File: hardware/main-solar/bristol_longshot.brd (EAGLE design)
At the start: 14 x 64 mm, 84 parts, among them U1 SAM_D20E, U10 SPV1040, U11 LT4054ES5-4.2, U12 TPS62243, U13 TPS62243, U14 TPS3808, U15 74LVC1G04GW, U2 SI4060, U3 UBLOX_MAX, U4 SST25WF040BT-40I/NP, U5 TG-5006CJ, U6 TG-5006CJ, U7 TPS3123, U8 SN74LVC1G32DCKR, U9 SE880, Y1 ABS05

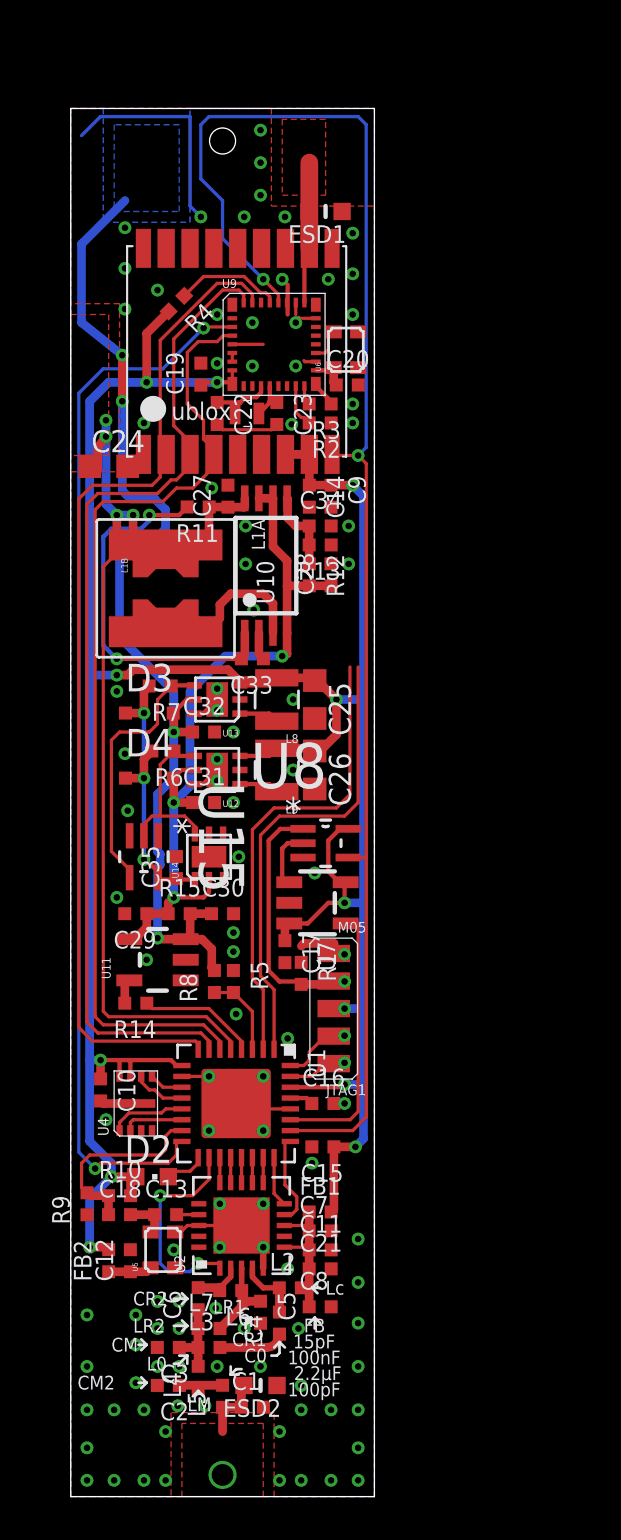
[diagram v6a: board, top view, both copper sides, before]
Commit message: Updated main tracker solar design to use a LTC3105 energy harvester for solar and a 3V primary lithium for backup. Work in Progress
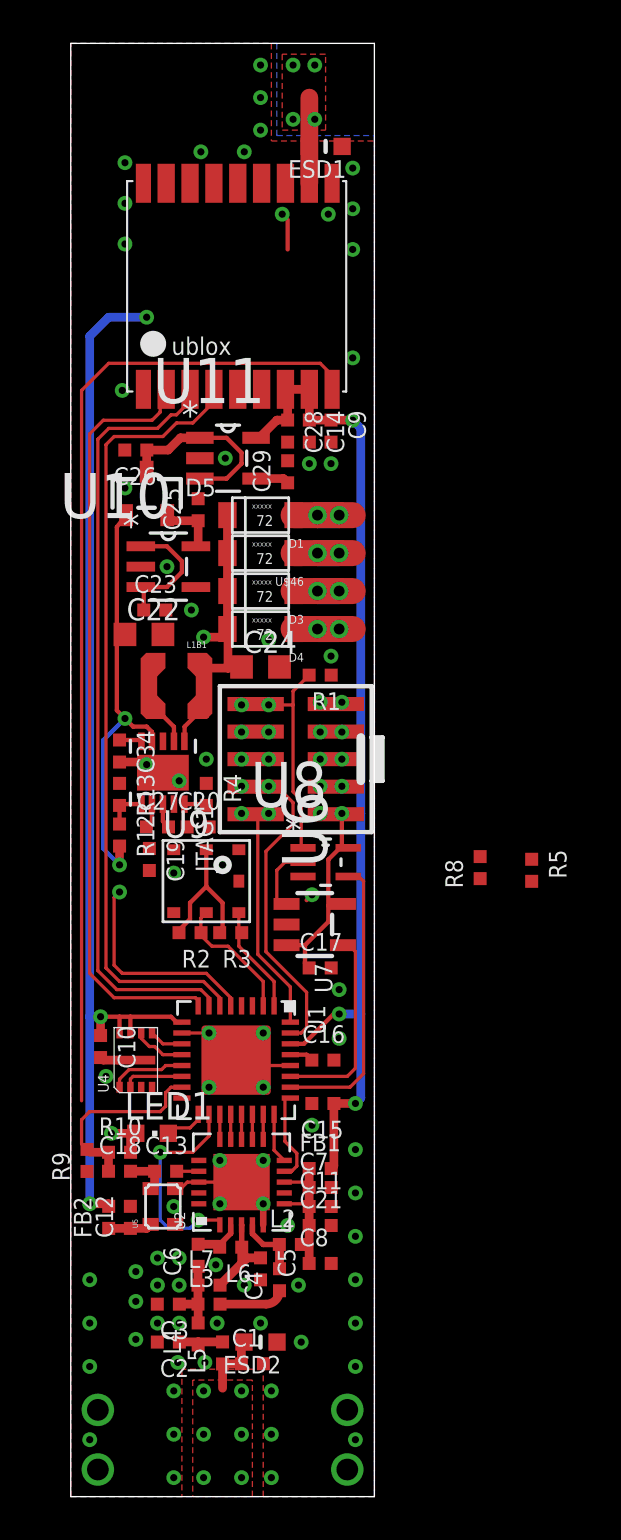
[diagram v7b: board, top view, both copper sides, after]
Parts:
- removed C30, C31, C32: 4.7µF, microbuilder_v3:_0402
- removed C33, C35: 1nF, microbuilder_v3:_0402
- removed D2: GREEN, led:CHIPLED_0603
- removed L1A: XAL6060, XAL6060:XAL60
- removed L1B: 10uH LPS3015, PecanFemto4:LPS3015
- removed L8, L9: 2.2µH, SparkFun:1007
- removed R11: 1kΩ, microbuilder_v3:_0402
- removed R14: 2.2kΩ, microbuilder_v3:_0402
- removed R15: 0Ω/DNP, microbuilder_v3:_0402
- removed R6, R7: 10kΩ, microbuilder_v3:_0402
- removed U12, U13: TPS62243, TPS62243:S-PWSON-N6
- removed U14: TPS3808, TPS3808:S-PWSON-N6
- removed U15: 74LVC1G04GW, 74LVC1G04GW_inverter:SOT65P210X110-5N
- removed Y1: ABS05, fbri:ABS05
- added D1, U$46: RB161M, RB161M:RB161M
- added D5: (no value), microbuilder_v3:SOT23-R
- added L1B1: 10uH LPS3015, PecanFemto4:LPS3015
- added LED1: GREEN, led:CHIPLED_0603
- C20: value 100nF -> 4.7µF
- C22: value 18pF -> 10µF; device microbuilder_v3:_0402 -> resistor:C0603K
- C23: value 18pF -> 1µF
- C25, C26: value 10µF -> 1µF; device resistor:C0603K -> microbuilder_v3:_0402
- C28: value 4.7µF -> 1µF
- C29: value 4.7µF -> 100nF
- C34: value 1nF -> 1µF
- D3, D4: value BAT760 -> RB161M; device BAT760:SOD323 -> RB161M:RB161M
- JTAG1: value M05 -> (none); device fbri:M05_SIDE -> microbuilder_v3:2X05_1.27MM_SMT
- R4: value 10kΩ -> 75kΩ
- U10: value SPV1040 -> LD6836TD/23P; device spv1040:TSSOP8 -> LD6836TD_23:SOT95P275X110-5N
- U11: value LT4054ES5-4.2 -> TPS73118DBVT; device XYKlib:SOT23-5 -> TPS73118DVBT:SOT95P280X145-5N
- U6: value TG-5006CJ -> LTC3105EDDPBF; device fbri:TC-5006CJ -> ltc3105:DFN300X300X80-11N
- U9: value SE880 -> BMP180; device fbri:SE880 -> SparkFun-Sensors:BMP180
- moved U9 24.9 mm to (6.25, 28.4)
- moved R3 24.7 mm to (7.38, 26.0)
- moved R2 24.3 mm to (5.50, 26.0)
- moved U11 23.4 mm to (7.25, 47.9), turned to 0 degrees
- moved R4 22.7 mm to (6.25, 32.4), turned to 270 degrees
- moved C19 22.5 mm to (3.62, 29.4), turned to 270 degrees
- moved C29 21.5 mm to (10.0, 47.2), turned to 90 degrees
- moved C20 21.5 mm to (5.88, 30.9)
- moved U6 21.2 mm to (4.25, 33.4)
- moved C26 16.9 mm to (3.00, 48.2), turned to 180 degrees
- moved C27 15.6 mm to (4.00, 30.9), turned to 0 degrees
- moved R12 14.9 mm to (2.25, 30.5)
- moved R13 14.8 mm to (2.25, 32.4), turned to 270 degrees
- moved R5 14.7 mm to (21.2, 28.9)
- moved C34 13.9 mm to (2.25, 34.4), turned to 270 degrees
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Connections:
- removed net BATTERY_BUCK_SW: L8.1, U13.1
- removed net BATTERY_EN: R7.1, U13.4, U15.4
- removed net CHG_STATUS: U11.1
- removed net CT: U14.3
- removed net LED2: D2.C, U1.17
- removed net LX1: L1A.P$2, L1B.2_1, L1B.2_2, L1B.2_3, L1B.2_4, L1B.2_5, L1B.2_6, L1B.2_7, L1B.2_8, L1B.2_9, U10.3
- removed net MPP-SET: C33.2, R11.2, U10.1
- removed net MPPT-VOUT-TANK: C28.1, C29.1, C31.1, D4.A, R12.2, R15.1, U10.4, U10.6, U10.7, U11.4, U12.5, U14.2
- removed net N$3: R3.2, U9.$17
- removed net N$5: R2.2, U9.$16
- removed net PROG: R14.2, U11.5
- removed net RTC_XI: C22.1, U9.$12, Y1.1
- removed net RTC_XO: C23.1, U9.$13, Y1.2
- removed net SE_MODE_PULL: R4.1, U9.$31
- removed net SE_ON_OFF: U1.16, U9.$3
- removed net SE_TCXO_CLK: U6.3, U9.$21
- removed net SE_VCO_TCXO: C20.1, U6.4, U9.$19
- removed net SE_VREG: U9.$6, U9.$7
- removed net SPV_VCTRL1: C34.1, R12.1, R13.2, U10.5
- removed net SUPERVISOR_VCC: C35.1, D3.C, D4.C, R6.2, R7.2, U14.1, U15.5
- removed net TANK_BUCK_SW: L9.1, U12.1
- removed net TANK_EN: R6.1, U12.4, U14.6, U15.2
- removed net VSOLAR: C24.1, C27.1, L1A.P$1, L1B.1_1, L1B.1_2, L1B.1_3, L1B.1_4, L1B.1_5, L1B.1_6, L1B.1_7, L1B.1_8, L1B.1_9, R11.1, U1.5, U10.8
- new net BATTERY_LDO_OUT: C25.1, D5.2, U10.5
- new net BATTERY_P: C23.1, U10.1, U10.3
- new net GPS_!RESET: U1.16, U3.9_V_RESET
- new net LED1: LED1.C, U1.17
- new net MPPT_AUX: C34.1, U6.10
- new net MPPT_FB: R12.1, R13.2, U6.1
- new net MPPT_LDO: C27.1, U6.2
- new net MPPT_SET: R4.2, U6.5
- new net MPPT_SW: L1B1.2_1, L1B1.2_2, L1B1.2_3, L1B1.2_4, L1B1.2_5, L1B1.2_6, L1B1.2_7, L1B1.2_8, L1B1.2_9, U6.7
- new net NR: C29.1, U11.4
- new net PANEL_1: D1.ANODE
- new net PANEL_2: U$46.ANODE
- new net PANEL_3: D3.ANODE
- new net PANEL_4: D4.ANODE
- new net SCHOTTY_COMB_OUT: C26.1, D5.3, U11.1, U11.3
- new net SOLAR: C24.1, D1.CATHODE, D3.CATHODE, D4.CATHODE, L1B1.1_1, L1B1.1_2, L1B1.1_3, L1B1.1_4, L1B1.1_5, L1B1.1_6, L1B1.1_7, L1B1.1_8, L1B1.1_9, U$46.CATHODE, U1.5, U6.6
- new net SOLAR_MPPT_OUT: C22.1, D5.1, R12.2, U6.9
- net !RESET: no longer U3.9_V_RESET, U9.$30
- net 1.8V: now also C20.1, C28.1, JTAG1.1, LED1.A, R2.2, R3.2, U11.5, U9.2, U9.3; no longer C25.1, C26.1, D2.A, JTAG1.$3, L8.2, L9.2, R4.2, U12.3, U13.3, U9.$8, U9.$9
- net BATTERY: no longer C30.1, C32.1, D3.A, R15.2, U11.3, U13.5
- net CHG_CONTROL: no longer R14.1
- net EXT!RESET: now also JTAG1.10; no longer JTAG1.$2
- net GIMO: no longer U9.$34
- net GND: now also JTAG1.3, JTAG1.5, R4.1, U6.11, U6.3, U9.7; no longer C30.2, C31.2, C32.2, C33.1, C35.2, JTAG1.$1, R2.1, R3.1, U12.2, U12.6, U12.PAD, U13.2, U13.6, U13.PAD, U14.5, U14.PAD, U15.3, U6.2, U9.$1, U9.$18, U9.$20, U9.$23, U9.$24, U9.$25, U9.$26, U9.$28, U9.$29, U9.$5
- net GOMI: no longer U9.$33
- net GPS_ANT: no longer U9.$27
- net SCL: now also R2.1, U9.5
- net SDA: now also R3.1, U9.6
- net SWDCLK: now also JTAG1.4; no longer JTAG1.$5
- net SWDIO: now also JTAG1.2; no longer JTAG1.$4
- net TIMEPULSE: no longer U9.$4
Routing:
- net !RESET: track 69.5 -> 13.3 mm, vias 2 -> 0
- net VSOLAR: track 53.3 -> 0.00 mm, vias 4 -> 0
- net BATTERY: track 49.3 -> 0.00 mm, vias 4 -> 0
- net SE_ON_OFF: track 49.3 -> 0.00 mm, vias 2 -> 0
- net GPS_!RESET: track 0.00 -> 45.7 mm
- net MPPT-VOUT-TANK: track 34.0 -> 0.00 mm, vias 3 -> 0
- net SOLAR: track 0.00 -> 26.7 mm, vias 0 -> 2
- net GND: track 39.6 -> 18.2 mm, vias 105 -> 85
- net SOLAR_MPPT_OUT: track 0.00 -> 20.3 mm, vias 0 -> 2
- net MPP-SET: track 17.5 -> 0.00 mm, vias 2 -> 0
- net 1.8V: track 137.5 -> 120.7 mm, vias 12 -> 9
- net SDA: track 21.5 -> 5.22 mm
- net SCL: track 21.4 -> 6.04 mm
- net SUPERVISOR_VCC: track 14.1 -> 0.00 mm, vias 3 -> 0
- net LX1: track 12.8 -> 0.00 mm
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- removed copper zone on layer 16, net BATTERY
- removed copper zone on layer 1, net VSOLAR
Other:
- board size 14 x 64 mm -> 14 x 67 mm
- board text added: "V0.xxx"
- board text removed: "+vbat"
- board text removed: "-vbat"
- board text removed: "2.2µF"
- board text removed: "C0"
- board text removed: "CM"
- board text removed: "CM2"
- board text removed: "CR1"
- board text removed: "CR2"
- board text removed: "FB 15pF 100nF 100pF"
- board text removed: "L0"
- board text removed: "LM"
- board text removed: "LR1"
- board text removed: "LR2"
- board text removed: "Lc"
- board text removed: "V0.981.1"

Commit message: More work on LTC3105 / primary 3V lithium board. Still work in progress
Needs solder pads and switch for 3V lithium battery.
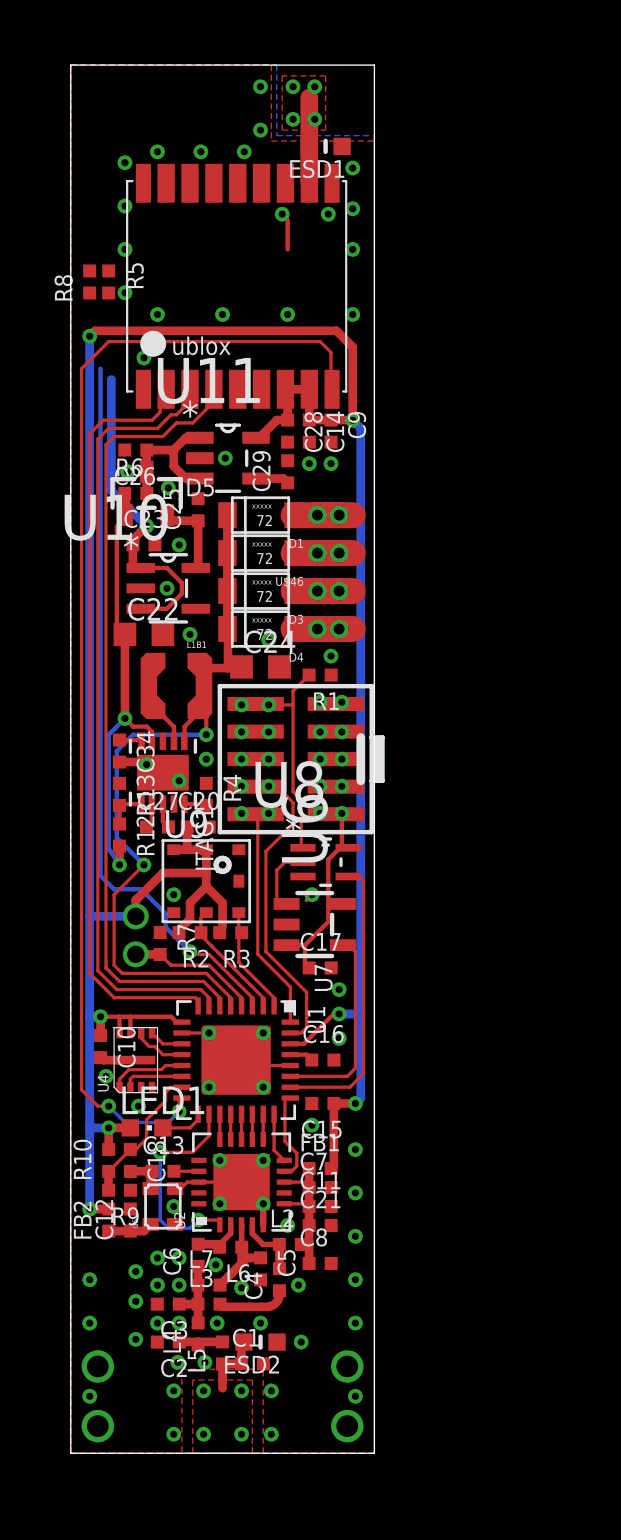
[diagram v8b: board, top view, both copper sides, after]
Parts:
- removed C19: 100nF, microbuilder_v3:_0402
- added R6: DNP, microbuilder_v3:_0402
- added R7: 100kΩ, microbuilder_v3:_0402
- R8: value 22kΩ -> 10kΩ
- moved R5 33.4 mm to (1.75, 56.0)
- moved R8 32.4 mm to (0.88, 56.0)
- moved C23 3.04 mm to (3.38, 43.9)
- moved R9 2.03 mm to (2.25, 14.1), turned to 180 degrees
- moved U10 1.00 mm to (4.50, 41.9)
- moved C18 0.71 mm to (2.75, 15.5), turned to 270 degrees
- moved R10 0.62 mm to (1.75, 15.5), turned to 90 degrees
- moved LED1 0.35 mm to (3.50, 17.0)
- moved C12 0.12 mm to (2.75, 12.8)
- moved C13 0.12 mm to (4.25, 15.0)
- moved FB2 0.12 mm to (1.75, 12.8)
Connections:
- net VBATT_SENSE renamed BATTERY_P_SENSE
- removed net BATTERY: R8.2
- removed net CHG_CONTROL: U1.4
- new net EXT_THERMISTOR_SENSE: R7.2, U1.4
- net 1.8V: no longer C19.1
- net BATTERY_P: now also R8.2
- net GND: now also R7.1; no longer C19.2
- net SCHOTTY_COMB_OUT: now also R6.2
- net SOLAR_MPPT_OUT: now also R6.1
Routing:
- net BATTERY_P_SENSE: track 0.00 -> 33.4 mm, vias 0 -> 1
- net 1.8V: track 120.7 -> 143.7 mm, vias 9 -> 10
- net SOLAR: track 26.7 -> 38.6 mm
- net BATTERY_P: track 5.98 -> 15.2 mm, vias 0 -> 1
- net GPS_!RESET: track 45.7 -> 53.2 mm, vias 0 -> 2
- net EXT_THERMISTOR_SENSE: track 0.00 -> 6.08 mm, vias 0 -> 1
- net SAM_XOSC: track 9.03 -> 6.60 mm
- net SCHOTTY_COMB_OUT: track 8.60 -> 6.88 mm
- net BATTERY_LDO_OUT: track 2.75 -> 3.75 mm
- net GND: vias 85 -> 88
- net ANT: vias 6 -> 4
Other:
- board size 14 x 67 mm -> 14 x 64 mm
- board text added: "10µH"
- board text added: "ARM SWD"
- board text added: "Atmel SAMD20"
- board text added: "BMP180"
- board text added: "External Thermistor"
- board text added: "LD6836TD"
- board text added: "LTC3105"
- board text added: "Solar"
- board text added: "TPS73118"
- board text removed: "ARM - SWD"
